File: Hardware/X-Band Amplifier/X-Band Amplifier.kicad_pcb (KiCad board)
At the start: 2 copper layers, 11 parts, among them J1 901-10513-3, J2 901-10513-3, U1 QPA1022

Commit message: Updating Board
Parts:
- removed H7, H8: 4-40, _tim-Mounting-Holes:2-56_Hole_Pad
- added TP1: TestPoint, TestPoint:TestPoint_Pad_D1.0mm, F.Cu at (144.0, 61.0)
- H5, H6: value 4-40 -> 2-56
- moved H5 95.7 mm to (137.2, 69.2)
- moved H6 15.5 mm to (142.2, 69.2)
- moved J2 0.14 mm to (152.3, 63.5)
- moved J1 0.13 mm to (127.0, 63.5)
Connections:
- U1 pad 16: unconnected-(U1-VDET-Pad16) -> Net-(U1-VDET)
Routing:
- net GND: track 0.00 -> 17.3 mm, vias 0 -> 25
- net Net-(J2-In): track 0.00 -> 10.2 mm
- net Net-(J1-In): track 0.00 -> 10.2 mm
- net Net-(U1-VDET): track 0.00 -> 3.53 mm
- net unconnected-(U1-VG-Pad19): track 0.00 -> 1.56 mm
- net unconnected-(U1-VD-Pad17): track 0.00 -> 1.29 mm
- added copper zone on B.Cu, net GND
- added copper zone on F.Cu, net GND
- added copper zone on In1.Cu, net GND
- added copper zone on In2.Cu, net GND
- added copper zone on F.Cu, net unconnected-(U1-VD-Pad17)
- added copper zone on F.Cu, net unconnected-(U1-VG-Pad19)
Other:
- board outline added: 25.4 x 25.4 mm
- copper layers 2 -> 4
- board text added: "${TITLE} ${REVISION} ${COMMENT1}"
- board text added: "VD"
- board text added: "VDET"
- board text added: "VG"

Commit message: Updated Board
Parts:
- moved TP1 1.30 mm to (144.9, 60.1)
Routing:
- net Net-(U1-VDET): track 3.53 -> 4.82 mm
- net GND: vias 25 -> 158
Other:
- board text added: "GND"
- board text added: "INPUT"
- board text added: "OUTPUT"

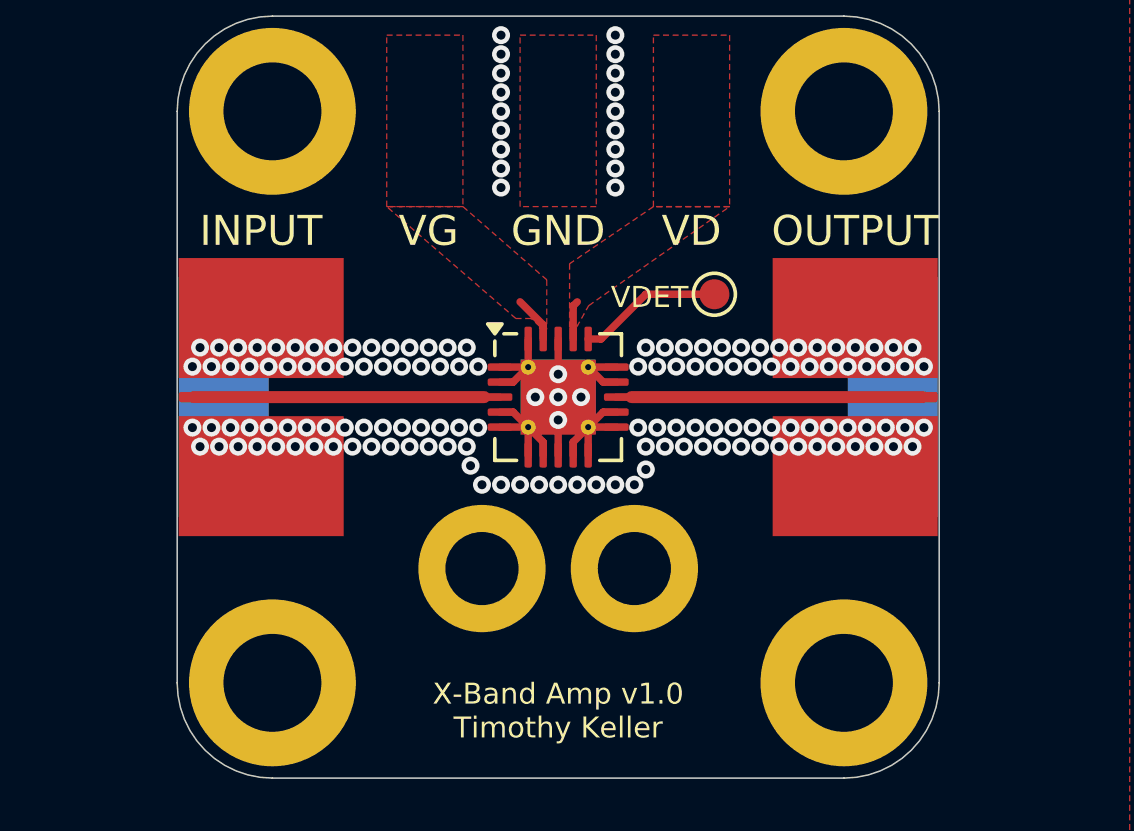
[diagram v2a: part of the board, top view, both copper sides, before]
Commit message: Adding capacitors
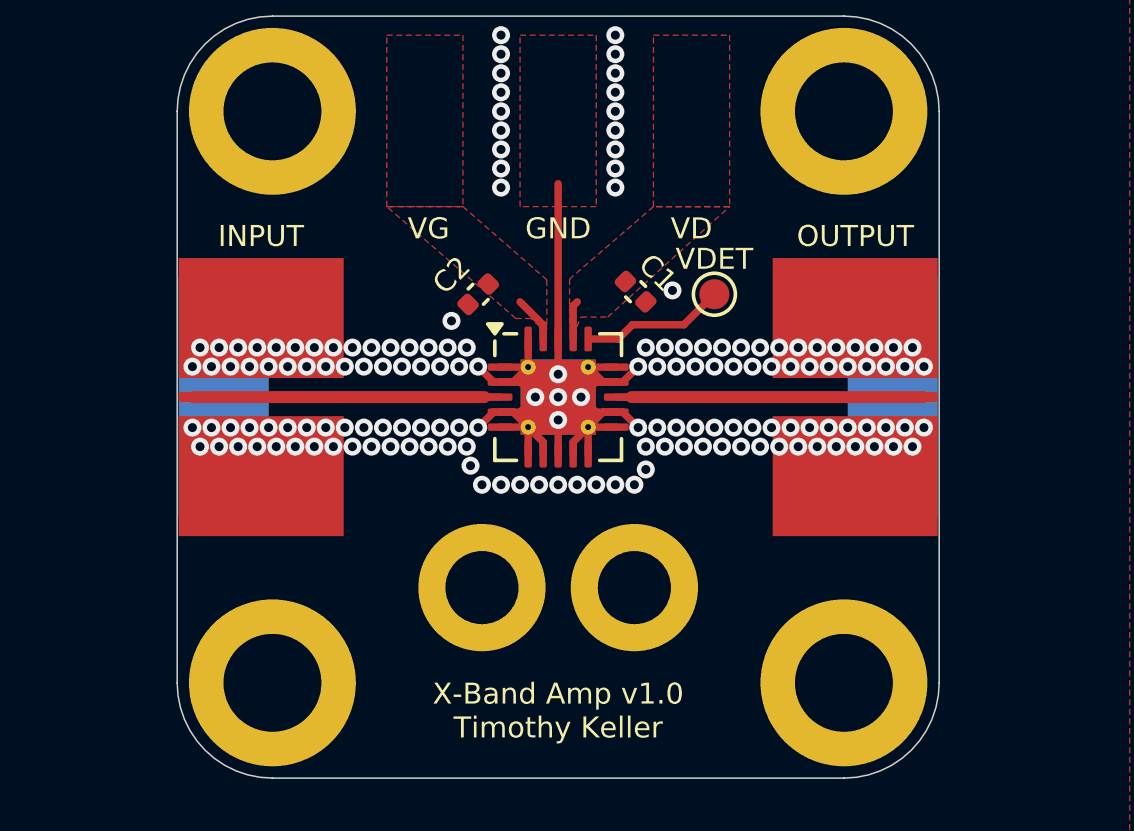
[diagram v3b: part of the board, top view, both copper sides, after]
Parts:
- added C1: 1nF, Capacitor_SMD:C_0402_1005Metric, F.Cu at (142.3, 60.0)
- added C2: 1nF, Capacitor_SMD:C_0402_1005Metric, F.Cu at (137.0, 60.1)
- moved H5 0.63 mm to (137.2, 69.8)
- moved H6 0.63 mm to (142.2, 69.8)
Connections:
- U1 pad 17: unconnected-(U1-VD-Pad17) -> VD
- U1 pad 19: unconnected-(U1-VG-Pad19) -> VG
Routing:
- net GND: track 17.3 -> 31.8 mm, vias 158 -> 160
- net unconnected-(U1-VG-Pad19): track 1.56 -> 0.00 mm
- net VG: track 0.00 -> 1.56 mm
- net unconnected-(U1-VD-Pad17): track 1.29 -> 0.00 mm
- net VD: track 0.00 -> 1.29 mm
- added copper zone on F.Cu, net VD
- added copper zone on F.Cu, net VG
- removed copper zone on F.Cu, net unconnected-(U1-VD-Pad17)
- removed copper zone on F.Cu, net unconnected-(U1-VG-Pad19)

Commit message: Adding GaN gate driver
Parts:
- moved C1 0.27 mm to (142.5, 60.0)
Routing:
- net GND: track 31.8 -> 32.7 mm
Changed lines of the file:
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@@
 			(outputformat 1)
 			(mirror no)
-			(drillshape 1)
+			(drillshape 0)
 			(scaleselection 1)
-			(outputdirectory "")
+			(outputdirectory "gerbers/")
 		)
 	)
@@
 			(size 1.08 1.08)
 			(layers "F.Paste")
-			(roundrect_rratio 0.231481)
+			(roundrect_rratio 0.2314805556)
 		)
 		(pad "" smd roundrect
@@
 			(size 1.08 1.08)
 			(layers "F.Paste")
-			(roundrect_rratio 0.231481)
+			(roundrect_rratio 0.2314805556)
 		)
 		(pad "" smd roundrect
@@
 			(size 1.08 1.08)
 			(layers "F.Paste")
-			(roundrect_rratio 0.231481)
+			(roundrect_rratio 0.2314805556)
 		)
 		(pad "" smd roundrect
@@
 			(size 1.08 1.08)
 			(layers "F.Paste")
-			(roundrect_rratio 0.231481)
+			(roundrect_rratio 0.2314805556)
 		)
 		(pad "1" smd roundrect
@@
 	(footprint "Capacitor_SMD:C_0402_1005Metric"
 		(layer "F.Cu")
-		(at 142.281589 59.985589 -45)
+		(at 142.5448 60.0456 -45)
 		(descr "Capacitor SMD 0402 (1005 Metric), square (rectangular) end terminal, IPC_7351 nominal, (Body size source: IPC-SM-782 page 76, https://www.pcb-3d.com/wordpress/wp-content/uploads/ipc-sm-782a_amendment_1_and_2.pdf), generated with kicad-footprint-generator")
 		(tags "capacitor")
@@
 	)
 	(segment
+		(start 143.5608 59.9186)
+		(end 143.350622 59.9186)
+		(width 0.2)
+		(layer "F.Cu")
+		(net 1)
+	)
+	(segment
 		(start 137.7625 64.5)
 		(end 138.7 64.5)
@@
 	)
 	(segment
+		(start 143.350622 59.9186)
+		(end 142.884211 60.385011)
+		(width 0.2)
+		(layer "F.Cu")
+		(net 1)
+	)
+	(segment
 		(start 138.2 64)
 		(end 138.7 64.5)
@@
 	)
 	(via
-		(at 143.51 59.944)
+		(at 143.5608 59.9186)
 		(size 0.6)
 		(drill 0.3)
@@
 	)
 	(segment
-		(start 143.891 61.087)
+		(start 141.42 61.57)
+		(end 141.918042 61.071958)
+		(width 0.25)
+		(layer "F.Cu")
+		(net 6)
+	)
+	(segment
+		(start 143.906042 61.071958)
 		(end 144.907 60.071)
 		(width 0.25)
@@
 	)
 	(segment
-		(start 141.701 61.5625)
-		(end 142.1765 61.087)
+		(start 141.918042 61.071958)
+		(end 143.906042 61.071958)
 		(width 0.25)
 		(layer "F.Cu")
@@
 	(segment
 		(start 140.7 61.5625)
-		(end 141.701 61.5625)
+		(end 141.4125 61.5625)
 		(width 0.25)
 		(layer "F.Cu")
@@
 	)
 	(segment
-		(start 142.1765 61.087)
-		(end 143.891 61.087)
+		(start 141.4125 61.5625)
+		(end 141.42 61.57)
 		(width 0.25)
 		(layer "F.Cu")
@@
 		(layer "F.Cu")
 		(hatch edge 0.5)
+		(priority 5)
+		(connect_pads yes
+			(clearance 0.254)
+		)
+		(min_thickness 0.25)
+		(filled_areas_thickness no)
+		(fill yes
+			(thermal_gap 0.5)
+			(thermal_bridge_width 0.5)
+		)
+		(polygon
+			(pts
+				(xy 144.018 59.055) (xy 141.097 61.722) (xy 141.097 62.23) (xy 146.558 62.23) (xy 146.558 59.055)
+			)
+		)
+	)
+	(zone
+		(net 1)
+		(net_name "GND")
+		(layer "F.Cu")
+		(hatch edge 0.5)
 		(connect_pads no
 			(clearance 0.5)
@@
 		(priority 4)
 		(connect_pads yes
-			(clearance 1.27)
+			(clearance 0.254)
 		)
 		(min_thickness 0.25)
